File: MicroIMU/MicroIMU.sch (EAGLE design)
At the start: 18 parts, among them IC1 LSM303DLHC

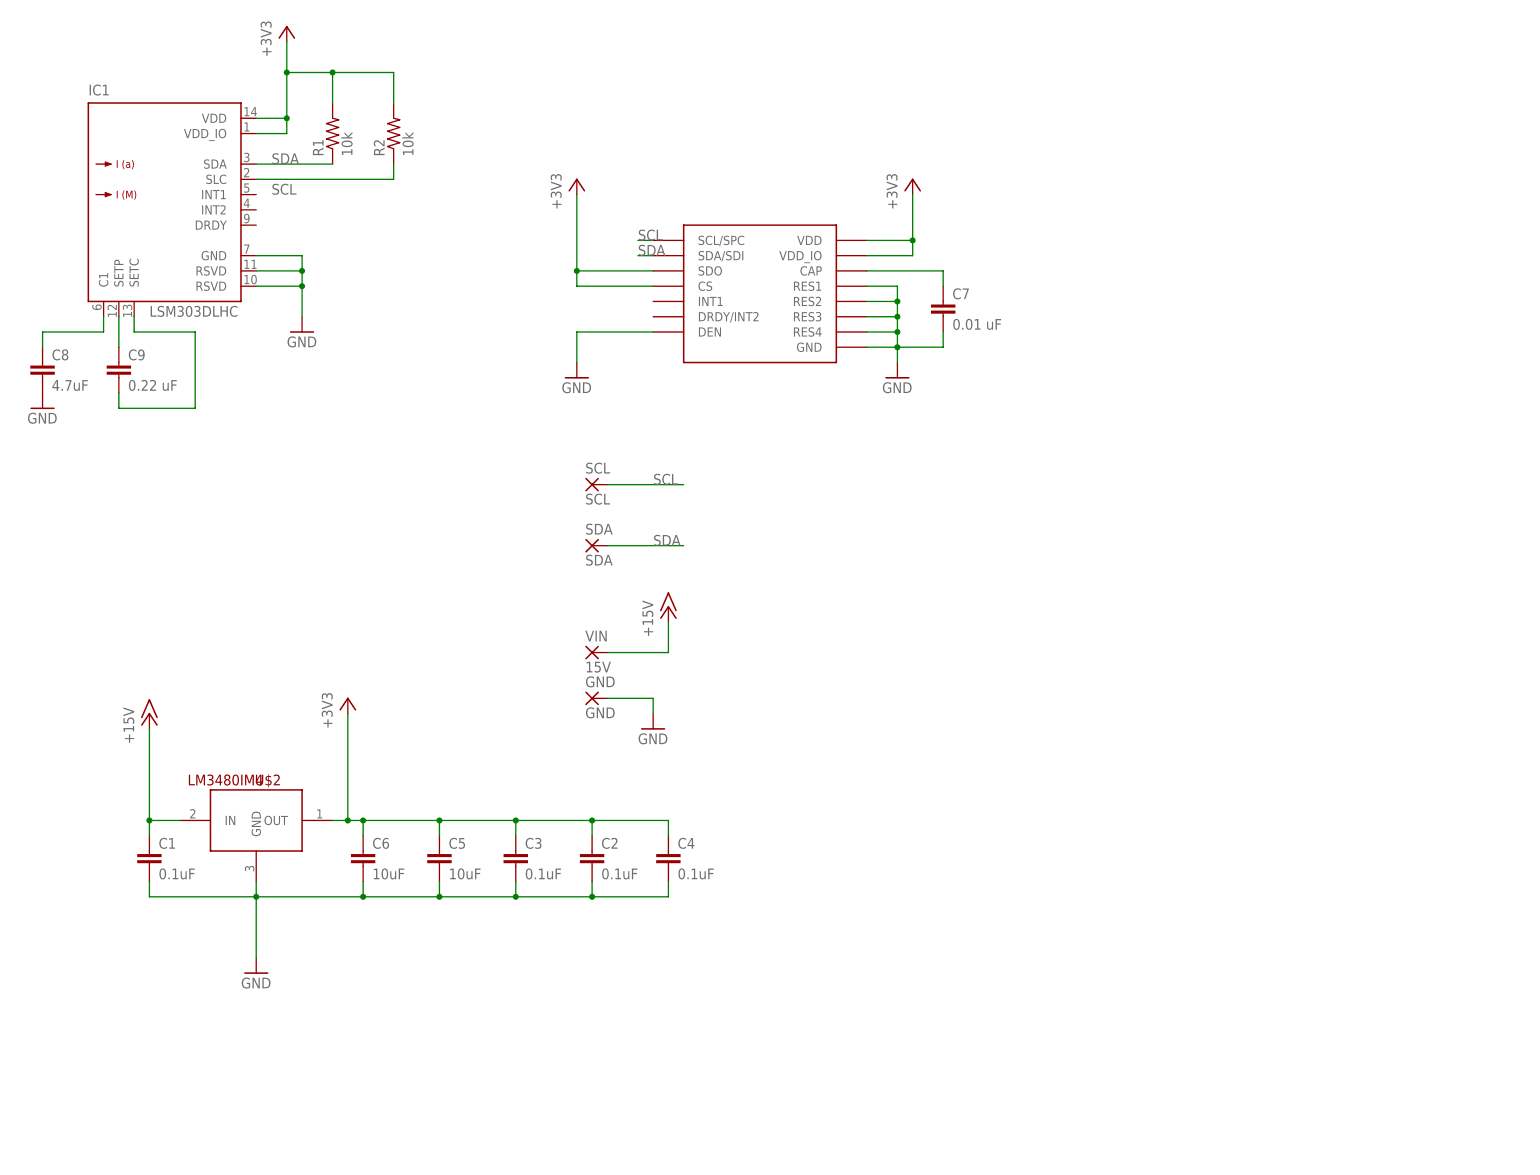
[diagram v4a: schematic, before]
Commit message: More rearrangement by Galen - everything is much closer together now
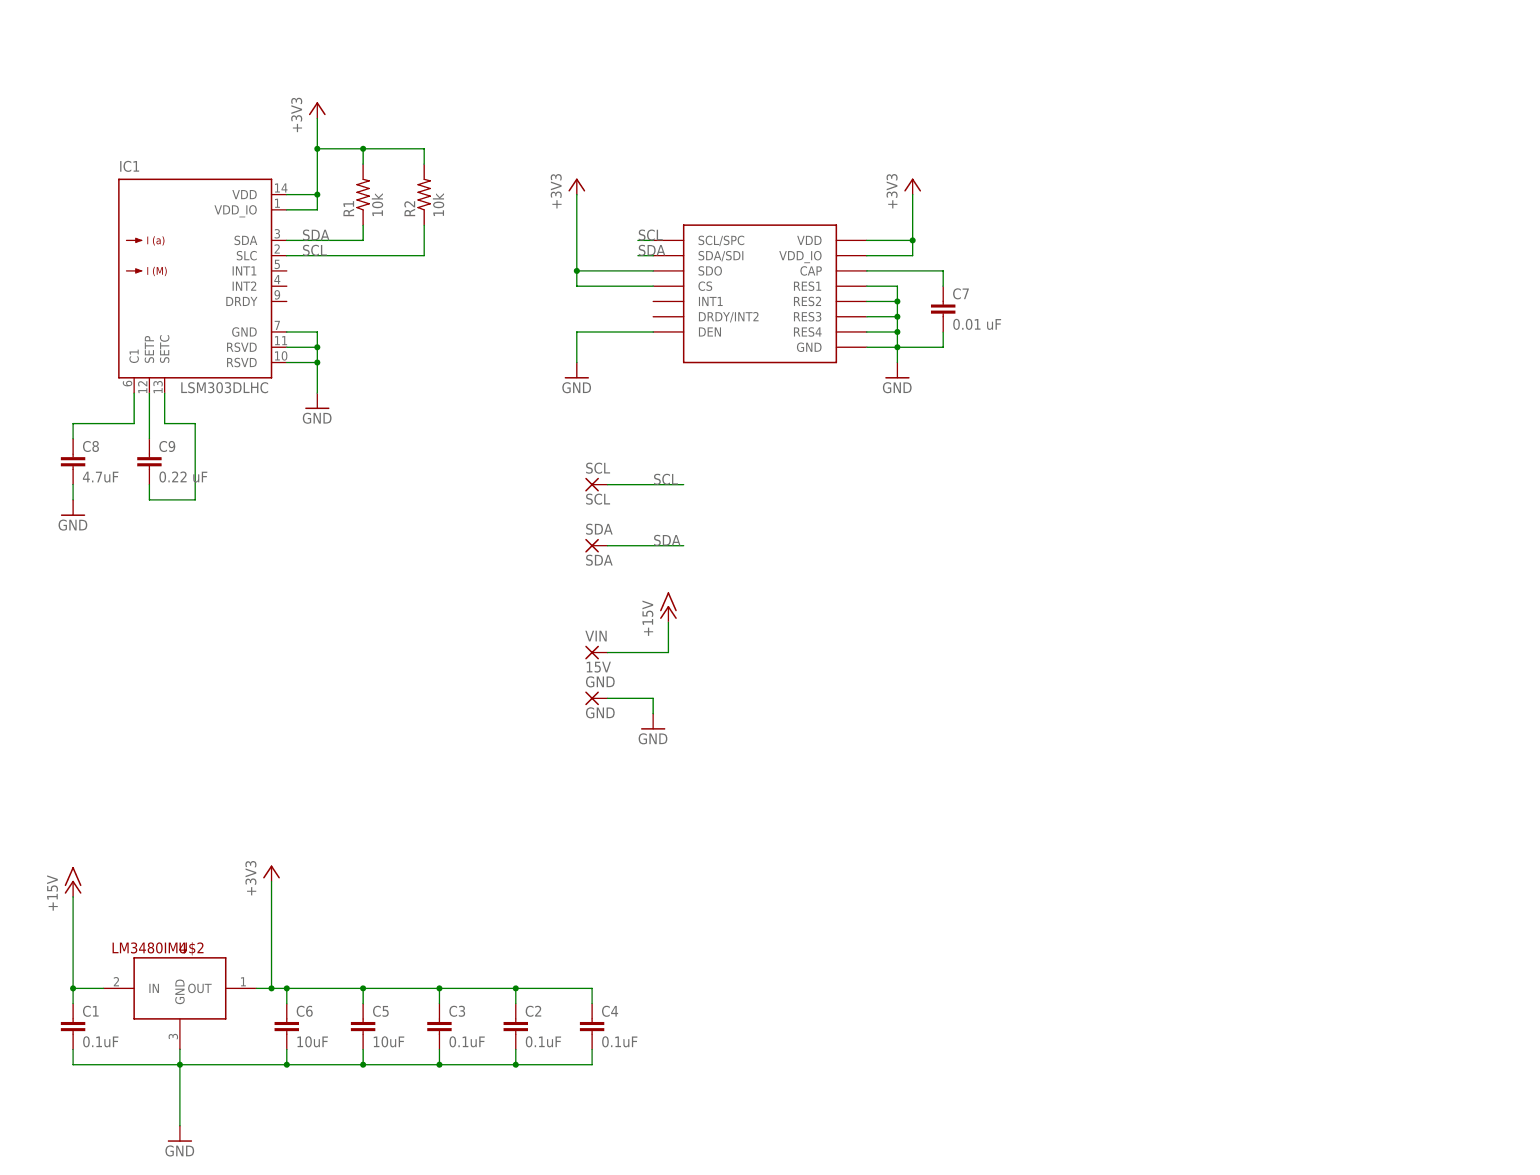
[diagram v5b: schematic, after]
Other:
- moved on the sheet: C1, C2, C3, C4, C5, C6, C8, C9, IC1, R1, R2, U$2

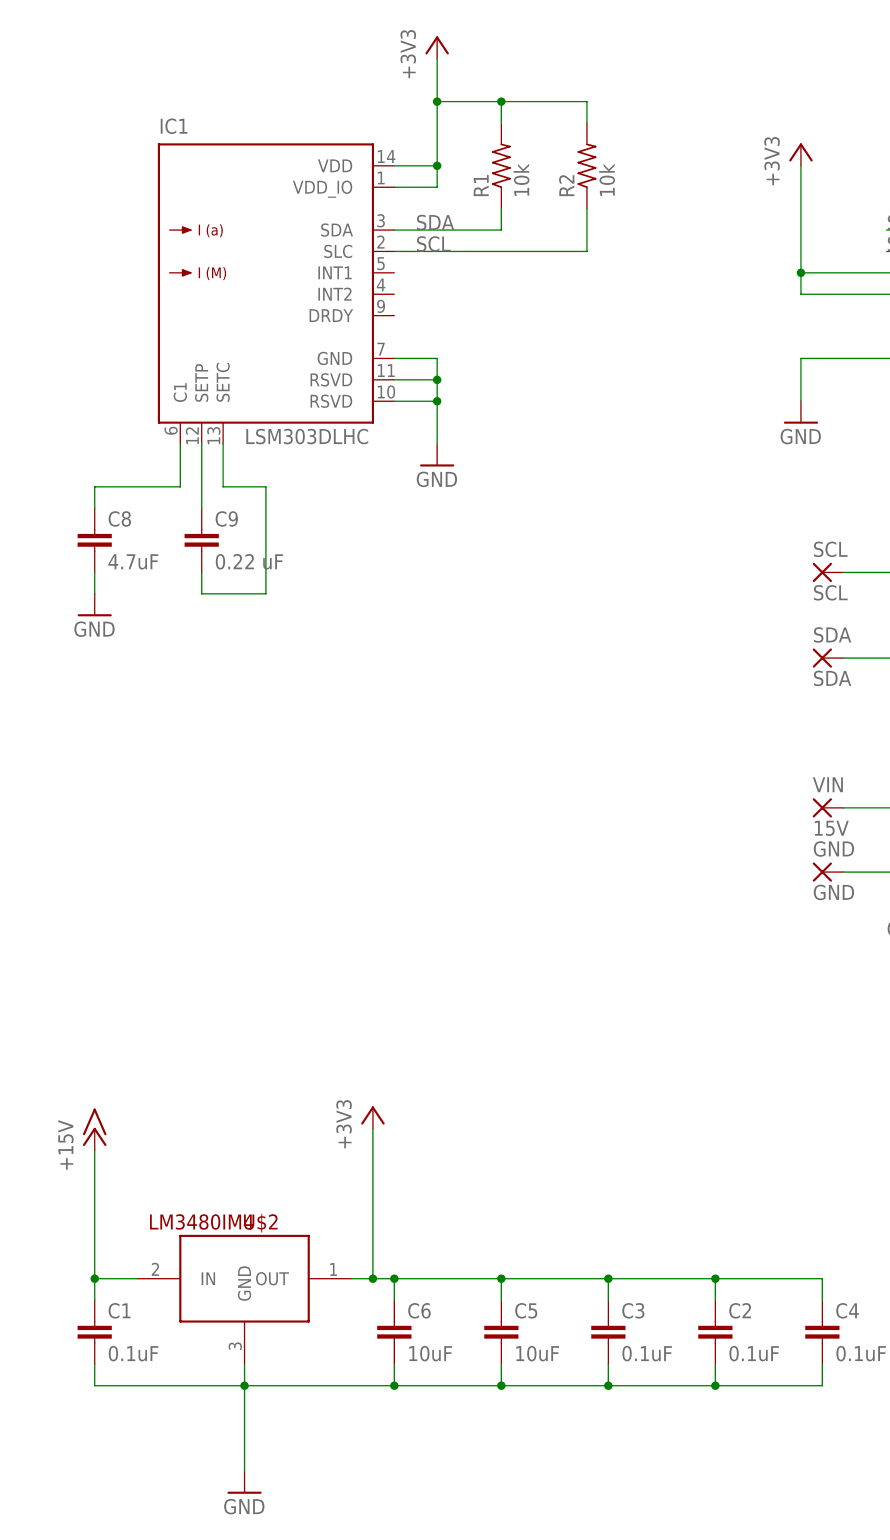
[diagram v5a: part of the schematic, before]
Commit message: Galen switched to LSM303D for accelerometer/compass - newer design with smaller package
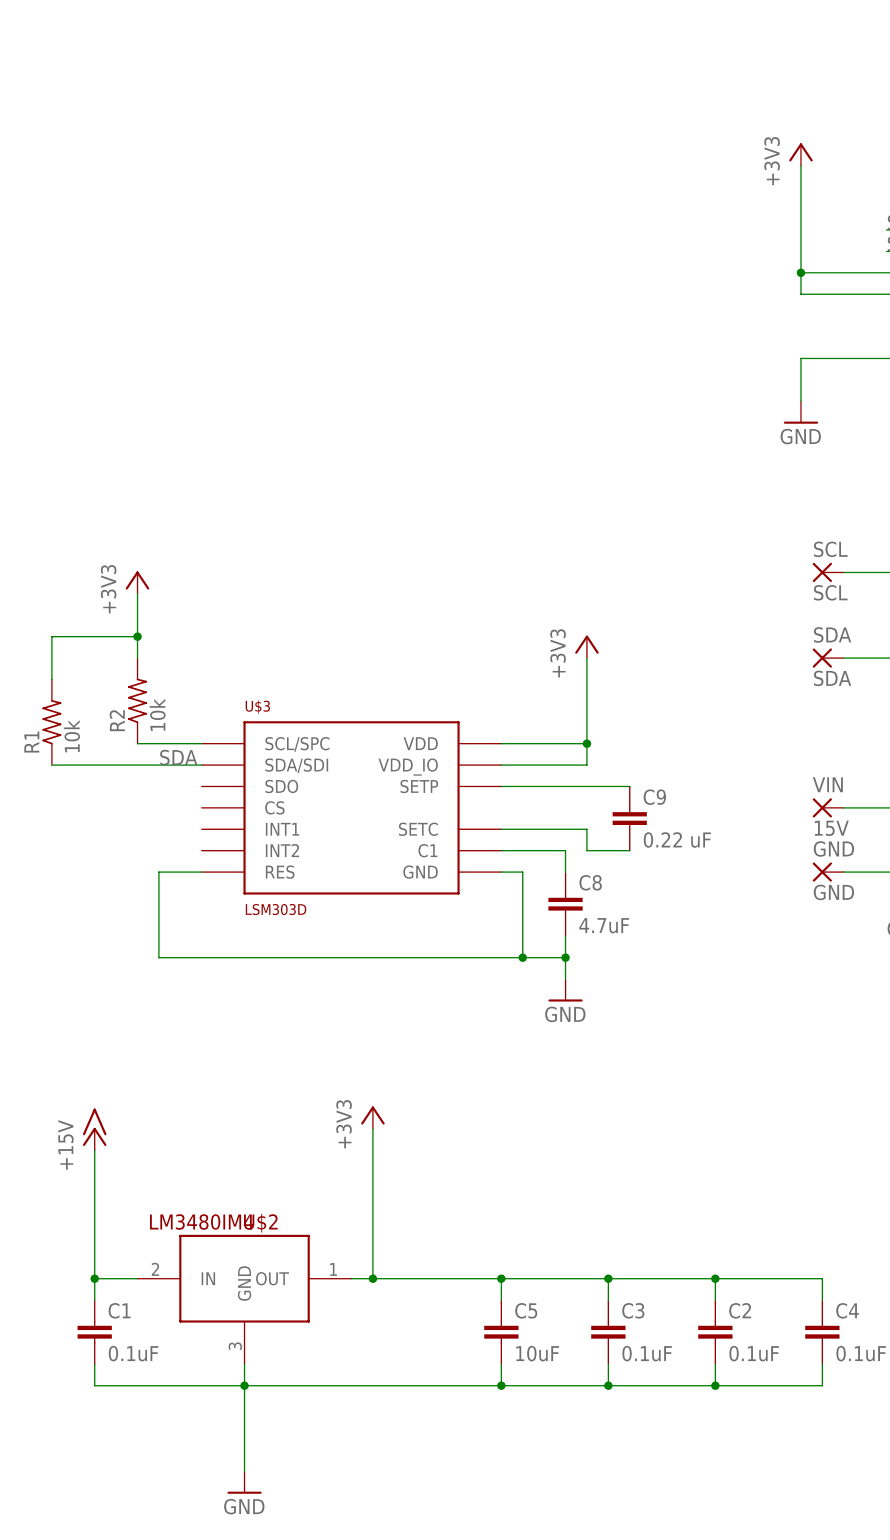
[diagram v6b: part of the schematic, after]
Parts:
- removed C6: 10uF, resistor:C-EUC0603
- removed IC1: LSM303DLHC, st-microelectronics:LSM303DLHC
- added U$3: LSM303D, st:LSM303D
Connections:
- net +3V3: now also U$3.VDD, U$3.VDD_IO; no longer C6.1, IC1.VDD, IC1.VDD_IO
- net GND: now also U$3.GND, U$3.RES; no longer C6.2, IC1.GND, IC1.RSVD@1, IC1.RSVD@2
- net N$1: now also U$3.C1; no longer IC1.C1
- net N$2: now also U$3.SETP; no longer IC1.SETP
- net N$3: now also U$3.SETC; no longer IC1.SETC
- net SCL: now also U$3.SCL/SPC; no longer IC1.SLC
- net SDA: now also U$3.SDA/SDI; no longer IC1.SDA
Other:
- moved on the sheet: C8, C9, R1, R2

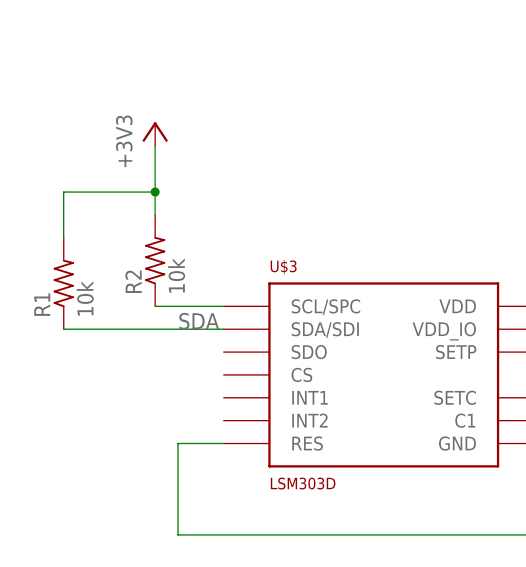
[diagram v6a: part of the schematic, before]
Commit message: Added missing connections for CS and SA0 on LSM303D
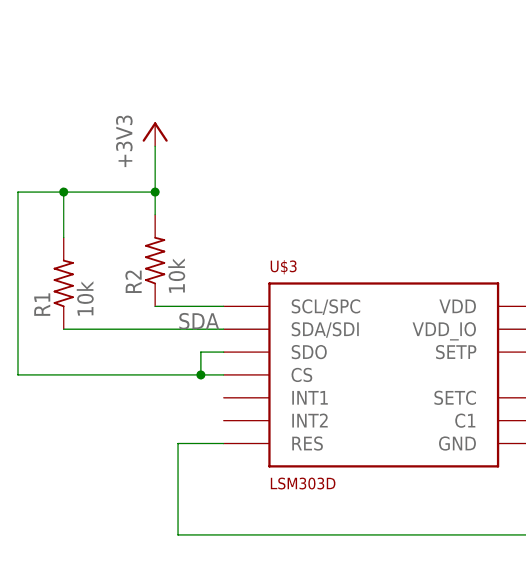
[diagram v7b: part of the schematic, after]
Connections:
- net +3V3: now also U$3.CS, U$3.SDO
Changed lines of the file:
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@@
 <wire x1="-5.08" y1="147.32" x2="5.08" y2="147.32" width="0.1524" layer="91"/>
 <junction x="5.08" y="147.32"/>
+<pinref part="U$3" gate="G$1" pin="CS"/>
+<wire x1="12.7" y1="127" x2="10.16" y2="127" width="0.1524" layer="91"/>
+<wire x1="10.16" y1="127" x2="-10.16" y2="127" width="0.1524" layer="91"/>
+<wire x1="-10.16" y1="127" x2="-10.16" y2="147.32" width="0.1524" layer="91"/>
+<wire x1="-10.16" y1="147.32" x2="-5.08" y2="147.32" width="0.1524" layer="91"/>
+<junction x="-5.08" y="147.32"/>
+<pinref part="U$3" gate="G$1" pin="SDO"/>
+<wire x1="12.7" y1="129.54" x2="10.16" y2="129.54" width="0.1524" layer="91"/>
+<wire x1="10.16" y1="129.54" x2="10.16" y2="127" width="0.1524" layer="91"/>
+<junction x="10.16" y="127"/>
 </segment>
 </net>
